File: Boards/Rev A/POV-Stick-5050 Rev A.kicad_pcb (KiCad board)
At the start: 2 copper layers, 23 parts, among them J1 ISP_Header, J2 Batt Conn, SW1 Power Switch, U1 ATTINY85-20SU, U10 APA102C, U11 APA102C, U2 APA102C, U3 APA102C, U4 APA102C, U5 APA102C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

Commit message: Created compact 5050 footprint
And I'll have to create other smaller footprints or select smaller components if I want this stick thing to look nice.
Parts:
- U10, U11, U2, U3, U4, U5, U6, U7, U8, U9: footprint LEDs:LED_RGB_5050-6 -> MyLEDs:LED_RGB_5050-6_Compact
- moved U2 20.7 mm to (143.8, 54.6)
- moved U3 18.4 mm to (150.4, 54.6)
- moved U4 16.1 mm to (157.0, 54.6)
- moved U5 13.9 mm to (163.6, 54.6)
- moved U6 11.6 mm to (170.2, 54.6)
- moved U7 9.29 mm to (176.8, 54.6)
- moved U8 7.01 mm to (183.4, 54.6)
- moved U9 4.73 mm to (190.0, 54.6)
- moved U10 2.46 mm to (196.6, 54.6)
- moved U11 0.45 mm to (203.2, 54.6)

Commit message: OSHPark settings, preliminary component locations
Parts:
- C2: footprint Capacitors_Tantalum_SMD:CP_Tantalum_Case-C_EIA-6032-28_Hand -> Capacitors_Tantalum_SMD:CP_Tantalum_Case-C_EIA-6032-28_Reflow
- D1: value Power LED -> Heartbeat LED
- moved C4 38.0 mm to (126.2, 56.9)
- moved D1 29.2 mm to (116.0, 55.9), turned to 0 degrees
- moved C3 29.1 mm to (116.1, 51.7)
- moved R1 28.1 mm to (109.6, 57.3)
- moved U1 26.9 mm to (120.9, 54.6)
- moved R3 25.6 mm to (116.0, 57.4), turned to 180 degrees
- moved R2 25.3 mm to (126.2, 51.4)
- moved S1 23.3 mm to (130.0, 57.9)
- moved C2 22.2 mm to (137.8, 54.6)
- moved C1 6.18 mm to (105.7, 54.4)
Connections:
- D1 pad 2: +BATT -> Net-(D1-Pad2)
- U1 pad 2: Net-(U1-Pad2) -> Net-(D1-Pad2)
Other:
- net class Default: clearance 0.2 -> 1.524; trace_width 0.25 -> 0.1524; via_dia 0.6 -> 0.508; via_drill 0.4 -> 0.254
- rule pad_to_mask_clearance: 0.2 -> 0.0508
- rule trace_clearance: 0.2 -> 1.524
- rule trace_min: 0.2 -> 0.1524
- rule via_min_drill: 0.3 -> 0.254
- rule via_min_size: 0.4 -> 0.508

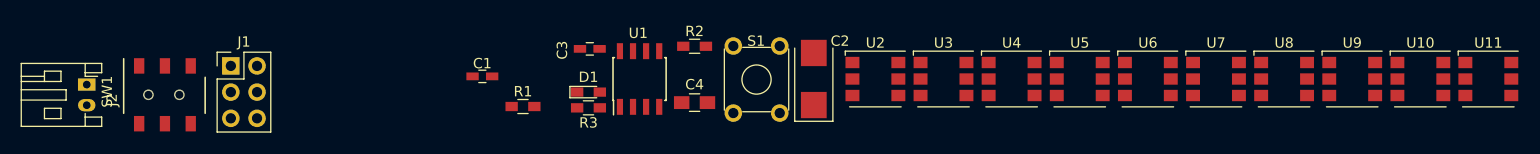
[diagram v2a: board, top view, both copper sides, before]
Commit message: Wired all non-power, added GND vias, prelim edge cut
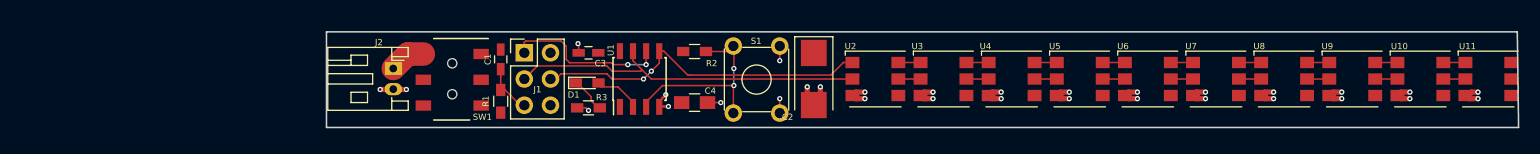
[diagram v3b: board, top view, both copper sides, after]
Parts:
- moved SW1 33.2 mm to (105.5, 52.2), turned to 270 degrees
- moved J2 29.8 mm to (97.0, 53.6)
- moved J1 28.5 mm to (109.7, 52.1)
- moved C1 2.43 mm to (107.4, 52.7), turned to 90 degrees
- moved R1 2.22 mm to (107.4, 56.8), turned to 90 degrees
- moved D1 0.90 mm to (115.8, 55.0)
- moved R2 0.51 mm to (126.2, 51.9)
- moved C3 0.40 mm to (116.0, 52.1), turned to 180 degrees
- turned C2 to 270 degrees
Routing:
- net GND: track 0.00 -> 41.4 mm, vias 0 -> 30
- net /SCK/WS2812Clock: track 0.00 -> 36.4 mm
- net /MOSI/WS2812Data: track 0.00 -> 33.8 mm, vias 0 -> 2
- net /PIN3/SW3: track 0.00 -> 19.1 mm, vias 0 -> 2
- net /PIN6/SCK: track 0.00 -> 15.9 mm, vias 0 -> 2
- net Net-(C1-Pad1): track 0.00 -> 5.07 mm
- net Net-(D1-Pad2): track 0.00 -> 4.26 mm
- net Net-(D1-Pad1): track 0.00 -> 4.25 mm
- net Net-(J2-Pad1): track 0.00 -> 3.50 mm
- net Net-(U7-Pad6): track 0.00 -> 2.15 mm
- net Net-(U7-Pad5): track 0.00 -> 2.15 mm
- net Net-(U5-Pad6): track 0.00 -> 2.15 mm
- net Net-(U5-Pad5): track 0.00 -> 2.15 mm
- net Net-(U3-Pad6): track 0.00 -> 2.15 mm
- net Net-(U3-Pad5): track 0.00 -> 2.15 mm
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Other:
- board outline added: 115.6 x 9.3 mm
- net class Default: clearance 1.524 -> 0.1524
- rule trace_clearance: 1.524 -> 0.1524

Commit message: Finished layout
Need to add Flamingo logo
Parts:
- J1: footprint Pin_Headers:Pin_Header_Straight_2x03_Pitch2.54mm -> MyConnectors:ISP_Header_Pogo_2x03_Pitch2.54mm; moved to B.Cu
- moved R2 5.21 mm to (126.2, 57.1)
- moved J1 5.08 mm to (109.9, 57.1)
- moved C4 4.95 mm to (126.4, 51.9)
- moved D1 0.92 mm to (116.1, 55.9)
- moved SW1 0.08 mm to (105.5, 52.1)
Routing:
- net Net-(C1-Pad1): track 5.07 -> 22.1 mm, vias 0 -> 4
- net /PIN3/SW3: track 19.1 -> 12.0 mm, vias 2 -> 0
- net Net-(J2-Pad1): track 3.50 -> 9.10 mm
- net GND: track 41.4 -> 45.0 mm, vias 30 -> 32
- net Net-(D1-Pad2): track 4.26 -> 6.00 mm
- net +BATT: track 0.00 -> 1.26 mm, vias 0 -> 1
- net Net-(D1-Pad1): track 4.25 -> 3.41 mm
- net /SCK/WS2812Clock: track 36.4 -> 35.6 mm, vias 0 -> 2
- net /MOSI/WS2812Data: track 33.8 -> 33.1 mm
- net (no net): track 0.54 -> 0.00 mm, vias 1 -> 0
- net /PIN6/SCK: track 15.9 -> 16.3 mm, vias 2 -> 1
- added copper zone on F.Cu, net +BATT
- added copper zone on B.Cu, net GND
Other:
- board size 115.6 x 9.3 mm -> 117.7 x 9.1 mm
- board text added: "POV Stick 5050 Rev A Paul Blackburn 2018 GitHub: @individual61"

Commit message: Final commit, as sent to OSHpark
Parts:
- added G***: LOGO, MyFlamingoLogo:flamingo_logo_8-8_6-7, B.Cu at (183.0, 54.6)
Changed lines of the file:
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@@
     (tracks 215)
     (zones 0)
-    (modules 23)
+    (modules 24)
     (nets 33)
   )
   (page A4)
   (layers
-    (0 F.Cu signal hide)
-    (31 B.Cu signal hide)
+    (0 F.Cu signal)
+    (31 B.Cu signal)
     (32 B.Adhes user)
     (33 F.Adhes user)
@@
     (41 Cmts.User user)
     (42 Eco1.User user)
-    (43 Eco2.User user hide)
+    (43 Eco2.User user)
     (44 Edge.Cuts user)
     (45 Margin user)
-    (46 B.CrtYd user hide)
-    (47 F.CrtYd user hide)
+    (46 B.CrtYd user)
+    (47 F.CrtYd user)
     (48 B.Fab user hide)
     (49 F.Fab user hide)
@@
       (net 2 GND))
   )
-  (gr_text "POV Stick 5050 Rev A\nPaul Blackburn 2018\nGitHub: @individual61" (at 134.874 54.61) (layer B.SilkS)
+  (module MyFlamingoLogo:flamingo_logo_8-8_6-7 (layer B.Cu)
+    (at 183.007 54.61 180)
+    (fp_text reference G*** (at -7.874 5.588 180) (layer B.SilkS) hide
+      (effects (font (thickness 0.3)) (justify mirror))
+    )
+    (fp_text value LOGO (at -2.286 5.461 180) (layer B.Fab) hide
+      (effects (font (thickness 0.3)) (justify mirror))
+    )
+    (fp_poly (pts (xy -1.216605 -1.420367) (xy -1.187211 -1.540498) (xy -1.17437 -1.755221) (xy -1.176753 -2.073721)
+      (xy -1.188625 -2.407055) (xy -1.204756 -2.758601) (xy -1.219814 -3.007051) (xy -1.23691 -3.170189)
+      (xy -1.259154 -3.265801) (xy -1.289656 -3.31167) (xy -1.331526 -3.325581) (xy -1.34936 -3.32619)
+      (xy -1.395319 -3.321326) (xy -1.426796 -3.294829) (xy -1.445367 -3.228846) (xy -1.452608 -3.105521)
+      (xy -1.450095 -2.907) (xy -1.439405 -2.615429) (xy -1.43052 -2.40684) (xy -1.41287 -2.082965)
+      (xy -1.390656 -1.800906) (xy -1.366188 -1.583274) (xy -1.341779 -1.452677) (xy -1.330364 -1.427126)
+      (xy -1.263879 -1.385639) (xy -1.216605 -1.420367)) (layer B.SilkS) (width 0.01))
+    (fp_poly (pts (xy 1.11547 -0.12071) (xy 1.192631 -0.254342) (xy 1.290431 -0.454313) (xy 1.36068 -0.612437)
+      (xy 1.478191 -0.901287) (xy 1.552262 -1.132814) (xy 1.594712 -1.357288) (xy 1.617356 -1.624979)
+      (xy 1.622222 -1.725068) (xy 1.62714 -2.021326) (xy 1.614723 -2.249862) (xy 1.586467 -2.386251)
+      (xy 1.581129 -2.396954) (xy 1.547541 -2.430361) (xy 1.526858 -2.380625) (xy 1.516434 -2.2341)
+      (xy 1.513744 -2.049326) (xy 1.486004 -1.527577) (xy 1.401696 -1.07513) (xy 1.252352 -0.65031)
+      (xy 1.210879 -0.558447) (xy 1.107469 -0.334833) (xy 1.049581 -0.197397) (xy 1.03057 -0.123191)
+      (xy 1.043795 -0.089268) (xy 1.071307 -0.076311) (xy 1.11547 -0.12071)) (layer B.SilkS) (width 0.01))
+    (fp_poly (pts (xy -1.01986 0.38375) (xy -0.837292 0.34526) (xy -0.658987 0.261944) (xy -0.559249 0.202269)
+      (xy -0.316384 0.059627) (xy -0.140215 -0.01719) (xy -0.000879 -0.035197) (xy 0.13149 -0.001407)
+      (xy 0.191154 0.026025) (xy 0.405142 0.107591) (xy 0.571174 0.103375) (xy 0.694096 0.038726)
+      (xy 0.762038 -0.020527) (xy 0.769584 -0.0835) (xy 0.714585 -0.191734) (xy 0.679191 -0.249567)
+      (xy 0.50974 -0.479523) (xy 0.30827 -0.652062) (xy 0.037625 -0.796125) (xy -0.090714 -0.849277)
+      (xy -0.319563 -0.945314) (xy -0.533705 -1.045214) (xy -0.651203 -1.107325) (xy -0.951932 -1.239713)
+      (xy -1.275114 -1.288112) (xy -1.656947 -1.25776) (xy -1.672814 -1.255171) (xy -1.984264 -1.229656)
+      (xy -2.289984 -1.265071) (xy -2.618419 -1.368393) (xy -2.998017 -1.5466) (xy -3.112727 -1.608326)
+      (xy -3.303453 -1.710238) (xy -3.45142 -1.783882) (xy -3.526239 -1.814176) (xy -3.52776 -1.814286)
+      (xy -3.559169 -1.762864) (xy -3.568095 -1.67695) (xy -3.529649 -1.520621) (xy -3.425193 -1.300804)
+      (xy -3.271053 -1.042613) (xy -3.083553 -0.771162) (xy -2.879018 -0.511568) (xy -2.673773 -0.288944)
+      (xy -2.652575 -0.268478) (xy -2.30749 0.029363) (xy -1.9904 0.230666) (xy -1.676025 0.347479)
+      (xy -1.339088 0.391852) (xy -1.26466 0.393095) (xy -1.01986 0.38375)) (layer B.SilkS) (width 0.01))
+    (fp_poly (pts (xy 1.153736 -0.695476) (xy 1.2298 -0.907363) (xy 1.251137 -1.09194) (xy 1.216761 -1.218411)
+      (xy 1.171618 -1.252773) (xy 1.095713 -1.225032) (xy 1.065785 -1.176895) (xy 1.044838 -1.061584)
+      (xy 1.033564 -0.87754) (xy 1.032991 -0.766125) (xy 1.037886 -0.453571) (xy 1.153736 -0.695476)) (layer B.SilkS) (width 0.01))
+    (fp_poly (pts (xy 0.965158 0.077052) (xy 0.967619 0.060476) (xy 0.946986 0.001572) (xy 0.94095 0)
+      (xy 0.889318 0.042378) (xy 0.876905 0.060476) (xy 0.8817 0.116204) (xy 0.903574 0.120952)
+      (xy 0.965158 0.077052)) (layer B.SilkS) (width 0.01))
+    (fp_poly (pts (xy 0.672277 0.332276) (xy 0.771948 0.25483) (xy 0.786191 0.205196) (xy 0.760439 0.133956)
+      (xy 0.740834 0.129188) (xy 0.650338 0.146219) (xy 0.559405 0.163632) (xy 0.460875 0.215016)
+      (xy 0.423545 0.292247) (xy 0.458236 0.352478) (xy 0.509102 0.362857) (xy 0.672277 0.332276)) (layer B.SilkS) (width 0.01))
+    (fp_poly (pts (xy 2.02535 2.453389) (xy 2.203869 2.40162) (xy 2.272809 2.325005) (xy 2.243167 2.208209)
+      (xy 2.224549 2.175664) (xy 2.182231 2.074721) (xy 2.220524 1.993471) (xy 2.290098 1.930958)
+      (xy 2.383588 1.836016) (xy 2.384606 1.761024) (xy 2.358288 1.72323) (xy 2.2588 1.645127)
+      (xy 2.149062 1.659866) (xy 2.006471 1.772687) (xy 1.965477 1.814286) (xy 1.823977 1.929966)
+      (xy 1.688073 1.99225) (xy 1.658957 1.995714) (xy 1.48741 1.938792) (xy 1.315887 1.781118)
+      (xy 1.156041 1.542333) (xy 1.019529 1.242076) (xy 0.918004 0.89999) (xy 0.878395 0.680357)
+      (xy 0.848947 0.489491) (xy 0.813032 0.396877) (xy 0.748663 0.380817) (xy 0.633854 0.419611)
+      (xy 0.619881 0.425218) (xy 0.514411 0.507938) (xy 0.48381 0.58891) (xy 0.504432 0.741105)
+      (xy 0.558579 0.967545) (xy 0.634672 1.23025) (xy 0.721128 1.491237) (xy 0.80637 1.712524)
+      (xy 0.861518 1.82778) (xy 1.054282 2.075524) (xy 1.312124 2.276011) (xy 1.601921 2.411434)
+      (xy 1.890548 2.463989) (xy 2.02535 2.453389)) (layer B.SilkS) (width 0.01))
+    (fp_poly (pts (xy 2.740544 1.36826) (xy 2.773002 1.244207) (xy 2.770618 1.199062) (xy 2.729415 1.041418)
+      (xy 2.657754 0.984852) (xy 2.572681 1.037513) (xy 2.539898 1.088762) (xy 2.502098 1.21649)
+      (xy 2.543209 1.304104) (xy 2.656766 1.391542) (xy 2.740544 1.36826)) (layer B.SilkS) (width 0.01))
+    (fp_poly (pts (xy 2.635391 1.730145) (xy 2.712991 1.652684) (xy 2.699667 1.545176) (xy 2.604452 1.453556)
+      (xy 2.443597 1.394741) (xy 2.344817 1.42889) (xy 2.329697 1.449223) (xy 2.339482 1.531161)
+      (xy 2.418392 1.629972) (xy 2.526917 1.70935) (xy 2.625548 1.732986) (xy 2.635391 1.730145)) (layer B.SilkS) (width 0.01))
+    (fp_poly (pts (xy 2.600477 1.905) (xy 2.570239 1.874762) (xy 2.54 1.905) (xy 2.570239 1.935238)
+      (xy 2.600477 1.905)) (layer B.SilkS) (width 0.01))
+    (fp_poly (pts (xy 2.194589 2.85486) (xy 2.262315 2.834468) (xy 2.485324 2.709211) (xy 2.680231 2.51717)
+      (xy 2.814295 2.296273) (xy 2.853988 2.149054) (xy 2.839297 2.000062) (xy 2.774122 1.946697)
+      (xy 2.687686 1.993612) (xy 2.62078 2.11192) (xy 2.48295 2.318759) (xy 2.266748 2.459463)
+      (xy 1.998632 2.528229) (xy 1.705062 2.519255) (xy 1.412496 2.426738) (xy 1.345596 2.391587)
+      (xy 1.178827 2.310622) (xy 1.102434 2.305747) (xy 1.117753 2.371191) (xy 1.226116 2.501183)
+      (xy 1.302806 2.576577) (xy 1.58711 2.777748) (xy 1.890942 2.872276) (xy 2.194589 2.85486)) (layer B.SilkS) (width 0.01))
+    (fp_poly (pts (xy 2.45722 2.224683) (xy 2.509762 2.177143) (xy 2.507788 2.121292) (xy 2.48804 2.116667)
+      (xy 2.38315 2.096577) (xy 2.332594 2.079695) (xy 2.264554 2.075343) (xy 2.273642 2.140171)
+      (xy 2.352929 2.224797) (xy 2.45722 2.224683)) (layer B.SilkS) (width 0.01))
+    (fp_poly (pts (xy 2.135455 2.999515) (xy 2.34657 2.961419) (xy 2.495882 2.905786) (xy 2.523476 2.884824)
+      (xy 2.580743 2.806662) (xy 2.552396 2.78738) (xy 2.459374 2.828618) (xy 2.39237 2.874542)
+      (xy 2.232913 2.93883) (xy 2.016804 2.961019) (xy 1.801467 2.93921) (xy 1.684178 2.897957)
+      (xy 1.572717 2.862898) (xy 1.515633 2.884013) (xy 1.540968 2.943144) (xy 1.574133 2.969216)
+      (xy 1.704953 3.00735) (xy 1.906822 3.016138) (xy 2.135455 2.999515)) (layer B.SilkS) (width 0.01))
+  )
+  (gr_text "POV Stick 5050 Rev A\nPaul Blackburn 2018\nGitHub: @individual61" (at 178.181 54.61) (layer B.SilkS)
     (effects (font (size 0.8 0.8) (thickness 0.15)) (justify left mirror))
   )
@@
     (connect_pads (clearance 0.1524))
     (min_thickness 0.1524)
-    (fill yes (arc_segments 16) (thermal_gap 0.408) (thermal_bridge_width 0.508) (smoothing chamfer))
+    (fill yes (arc_segments 16) (thermal_gap 0.308) (thermal_bridge_width 0.508) (smoothing chamfer))
     (polygon
       (pts

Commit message: Added text "wrong footprint" for aTtINY85
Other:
- board text added: "WRONG FOOTPRINT"
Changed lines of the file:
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@@
     (links 70)
     (no_connects 1)
-    (area 90.475999 49.962999 208.355001 59.257001)
+    (area 89.1306 47.6528 208.355001 60.6174)
     (thickness 1.6)
-    (drawings 8)
+    (drawings 9)
     (tracks 215)
     (zones 0)
@@
   (layers
     (0 F.Cu signal)
-    (31 B.Cu signal)
+    (31 B.Cu signal hide)
     (32 B.Adhes user)
     (33 F.Adhes user)
@@
     (42 Eco1.User user)
     (43 Eco2.User user)
-    (44 Edge.Cuts user)
-    (45 Margin user)
-    (46 B.CrtYd user)
-    (47 F.CrtYd user)
+    (44 Edge.Cuts user hide)
+    (45 Margin user hide)
+    (46 B.CrtYd user hide)
+    (47 F.CrtYd user hide)
     (48 B.Fab user hide)
-    (49 F.Fab user hide)
+    (49 F.Fab user)
   )
   (setup
@@
       (xy 1.704953 3.00735) (xy 1.906822 3.016138) (xy 2.135455 2.999515)) (layer B.SilkS) (width 0.01))
   )
+  (gr_text "WRONG FOOTPRINT" (at 121.666 46.355) (layer Dwgs.User)
+    (effects (font (size 1.5 1.5) (thickness 0.3)))
+  )
   (gr_text "POV Stick 5050 Rev A\nPaul Blackburn 2018\nGitHub: @individual61" (at 178.181 54.61) (layer B.SilkS)
